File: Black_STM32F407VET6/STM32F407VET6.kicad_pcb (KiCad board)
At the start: 2 copper layers, 96 parts, among them J1 T0, J10 - HotBed +, J11 Heater0, J12 X-, J13 Y-, J14 Z-, J15 Z+, J16 USB_B, J17 LeftSpi, J18 EXTRAPINS, J2 T1, J23 EXP2, J24 LCD2004, J25 Bottom, J26 Right, J28 LIGHTS, J29 Z, J3 TB, J30 Z, J38 X, J39 Y, J4 TC, J41 E0, J43 Heater1, J44 COM, J47 I2C, J48 SPI, J49 SPI, J5 + VIN -, J50 SDIO, J51 Servo, J52 Servo, J53 PowerSelect, J54 Power, J55 PD11, J56 Power, J6 Fan3, J7 Fan2, J8 Fan1, J9 Fan0, Q1 BCX70, Q10 BCX70, Q11 BCX70, Q12 IRLR8726PBF, Q13 IRLR8726PBF, Q14 IRLR8726PBF, Q2 BCX70, Q3 BCX70, Q4 IRLML0030TRPBF, Q5 BCX70, Q6 IRLML0030TRPBF, Q7 IRLML0030TRPBF, Q8 IRLML0030TRPBF, Q9 BCX70, SW1 Boot0, U1 LeftAnalog, U2 Left5V, U5 AT24CS01-SSHM

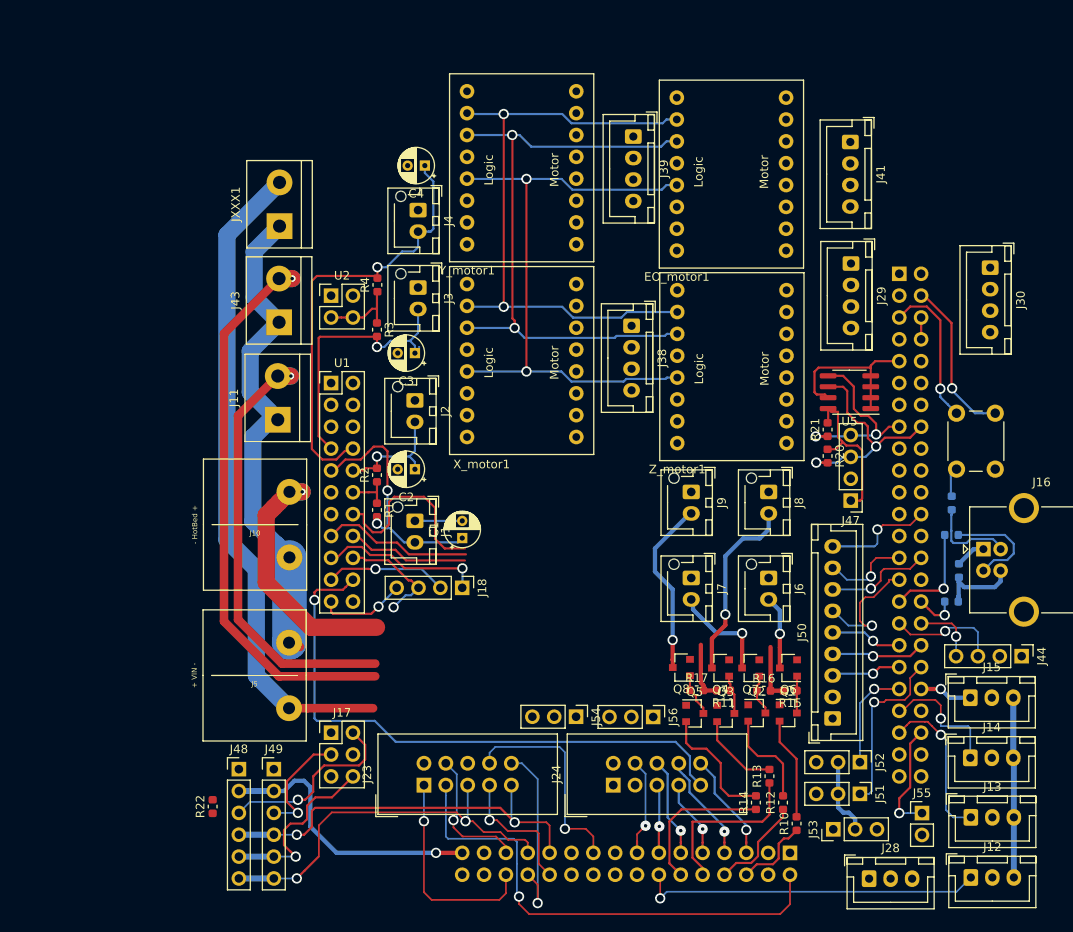
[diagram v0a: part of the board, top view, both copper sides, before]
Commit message: Wider tracks, more clearance, X & Y logic. 	SPI 1 is no longer used on shield because is used on the mcu board with different pins 	Added a design rule, distance between tracks is now at least 0.2925 	Wired X and Y driver logic with pin changes. 	Added a buck convertor spot with external connections in the meantime 	Stepper drivers are now consistently spaced from each other.
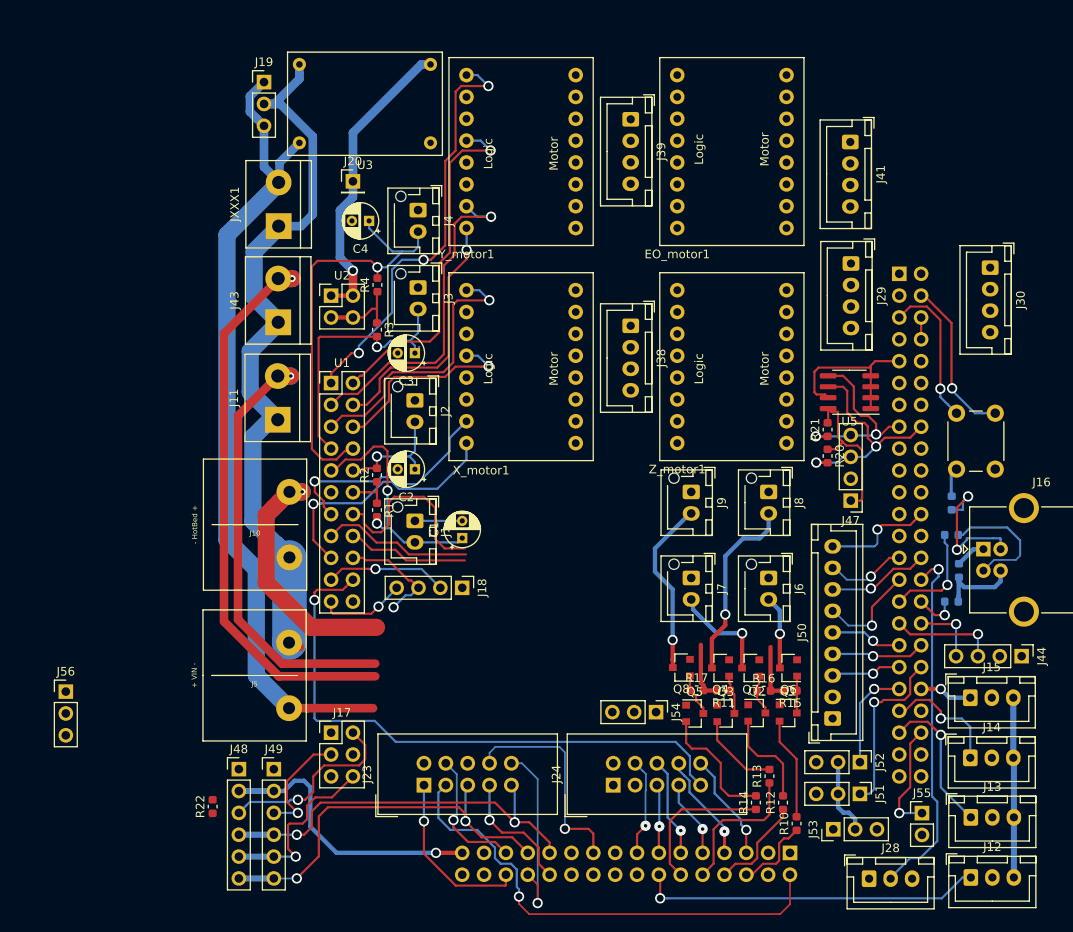
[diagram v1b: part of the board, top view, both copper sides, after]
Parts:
- added J19: 12Vinput, Connector_PinHeader_2.54mm:PinHeader_1x03_P2.54mm_Vertical, F.Cu at (114.1, 61.5)
- added J20: 5VOut, Connector_PinHeader_2.54mm:PinHeader_1x01_P2.54mm_Vertical, F.Cu at (124.5, 73.1)
- added U3: BuckConvertor, Motor_driver:MP2307Buck, F.Cu at (125.9, 64.1)
- moved J56 68.3 mm to (91.1, 132.4), turned to 0 degrees
- moved J54 9.31 mm to (159.7, 134.8)
- moved C4 9.12 mm to (126.3, 77.7)
- moved EO_motor1 2.62 mm to (160.1, 80.5)
- moved J39 2.03 mm to (156.7, 65.9)
- moved Y_motor1 1.89 mm to (135.6, 80.5)
- moved X_motor1 0.71 mm to (135.6, 105.5)
- moved JXXX1 0.10 mm to (115.8, 78.3)
- moved J43 0.10 mm to (115.8, 89.5)
- moved J38 0.10 mm to (156.7, 89.9)
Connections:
- J10 pad 1: Net-(J10-Pad1) -> 12V
- J18 pad 1: PA4 -> PD6
- J26 pad 20: Y_En -> PD6
- Q12 pad 2: Net-(Q12-Pad2) -> Net-(J10-Pad2)
- U1 pad 1: X_Step -> Y_En
- U1 pad 13: X_Dir -> X_Step
- U1 pad 17: PA4 -> X_Dir
- U1 pad 3: X_CS -> Y_Step
- U1 pad 4: Y_Step -> Y_Dir
- U1 pad 6: Y_Dir -> X_CS
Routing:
- net CLK: track 119.9 -> 46.3 mm, vias 4 -> 2
- net MISO: track 116.4 -> 43.4 mm, vias 4 -> 2
- net MOSI: track 118.6 -> 46.7 mm, vias 4 -> 2
- net Y_En: track 0.00 -> 49.5 mm, vias 0 -> 3
- net LIGHT_DIN: track 0.00 -> 42.0 mm, vias 0 -> 1
- net Y_CS: track 0.00 -> 41.3 mm, vias 0 -> 1
- net Y_Step: track 0.00 -> 39.2 mm, vias 0 -> 1
- net 5V: track 24.5 -> 59.5 mm, vias 0 -> 1
- net X_En: track 0.00 -> 32.6 mm, vias 0 -> 1
- net X_Dir: track 0.04 -> 30.3 mm, vias 0 -> 1
- net Y_Dir: track 0.00 -> 30.1 mm, vias 0 -> 1
- net 12V: track 132.6 -> 160.4 mm
- net X_Step: track 0.00 -> 26.7 mm, vias 0 -> 1
- net GND: track 114.3 -> 140.3 mm, vias 0 -> 2
- net X_CS: track 0.00 -> 23.0 mm, vias 0 -> 1
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
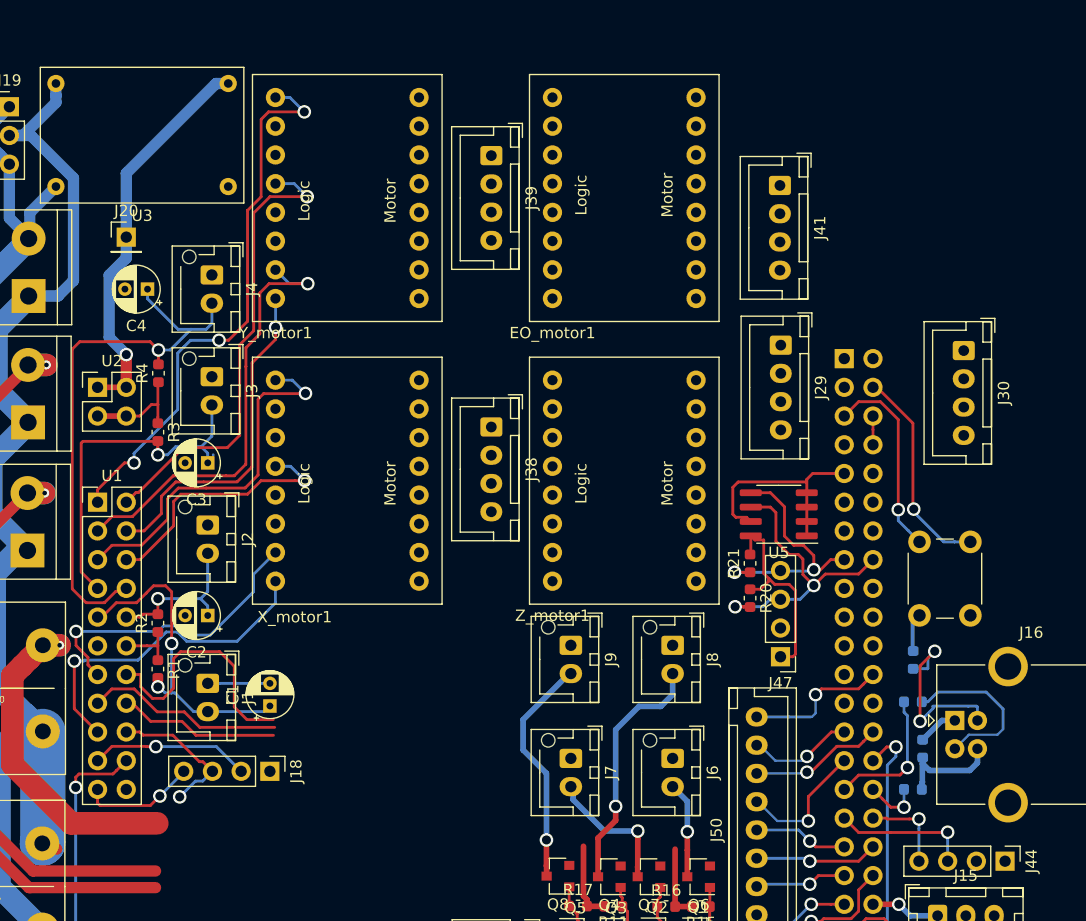
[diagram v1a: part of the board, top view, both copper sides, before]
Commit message: Z and E0 wiring 	- 12V rails 	- TODO: spi lines
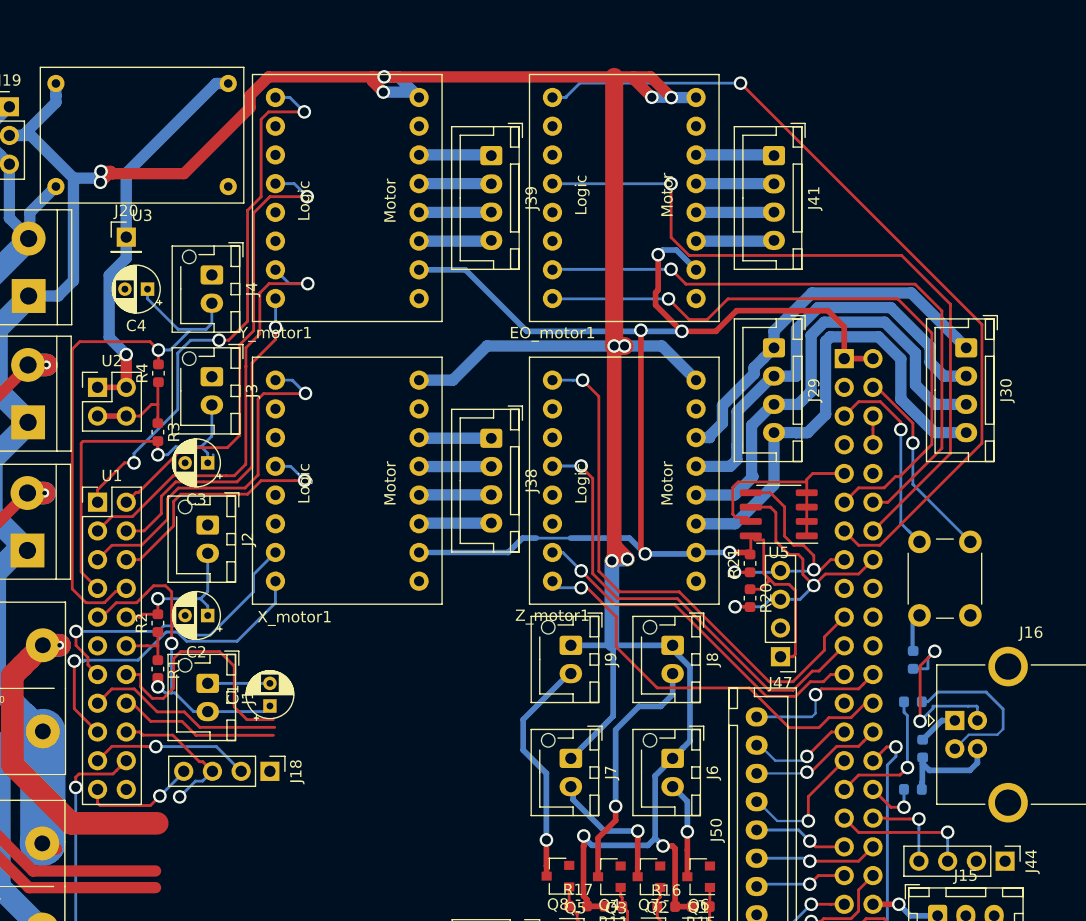
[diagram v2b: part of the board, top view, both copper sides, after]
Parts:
- moved J41 2.69 mm to (181.7, 65.9)
- moved J38 1.00 mm to (156.7, 90.9)
- moved J29 0.65 mm to (181.7, 82.9)
- moved J30 0.33 mm to (198.7, 82.9)
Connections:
- J26 pad 11: Z_En -> E0_Dir
- J26 pad 12: E0_En -> E0_Step
- J26 pad 13: Z_CS -> E0_En
- J26 pad 19: E0_Step -> Z_En
- J26 pad 21: Z_Step -> Z_CS
- J26 pad 23: E0_Dir -> Z_Step
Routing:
- net 12V: track 160.4 -> 367.1 mm, vias 1 -> 13
- net 3V3: track 84.7 -> 192.5 mm, vias 2 -> 7
- net E0_En: track 0.00 -> 74.3 mm, vias 0 -> 1
- net E0_CS: track 0.00 -> 65.3 mm, vias 0 -> 1
- net E0_Step: track 0.00 -> 56.2 mm, vias 0 -> 1
- net E0_Dir: track 0.00 -> 56.1 mm, vias 0 -> 1
- net Z_En: track 0.00 -> 49.0 mm, vias 0 -> 1
- net Net-(J29-Pad4): track 0.00 -> 42.8 mm
- net Net-(J29-Pad3): track 0.00 -> 40.6 mm
- net Z_CS: track 0.00 -> 40.6 mm, vias 0 -> 1
- net Net-(J29-Pad2): track 0.00 -> 37.9 mm
- net Z_Dir: track 0.00 -> 36.2 mm, vias 0 -> 1
- net Net-(J29-Pad1): track 0.00 -> 33.4 mm
- net Z_Step: track 0.00 -> 31.9 mm, vias 0 -> 1
- net Net-(EO_motor1-Pad14): track 0.00 -> 6.92 mm
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
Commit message: Power lines
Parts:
- moved C9 95.7 mm to (77.8, 134.8), turned to 270 degrees
- moved Q12 94.8 mm to (152.6, 113.9), turned to 0 degrees
- moved Q14 90.5 mm to (152.6, 120.9), turned to 0 degrees
- moved Q9 88.9 mm to (148.8, 115.7), turned to 270 degrees
- moved R28 87.9 mm to (151.4, 122.8), turned to 90 degrees
- moved R26 87.4 mm to (149.3, 119.0), turned to 270 degrees
- moved Q13 87.2 mm to (152.6, 127.9), turned to 0 degrees
- moved R25 85.4 mm to (147.8, 119.0), turned to 270 degrees
- moved Q11 84.8 mm to (148.8, 122.3), turned to 270 degrees
- moved R27 81.6 mm to (147.8, 125.9), turned to 90 degrees
- moved Q10 81.4 mm to (148.8, 129.4), turned to 270 degrees
- moved R23 71.3 mm to (142.7, 117.2)
- moved R24 71.3 mm to (142.7, 115.4)
- moved J56 54.2 mm to (145.2, 135.1), turned to 90 degrees
- moved C10 22.8 mm to (68.8, 134.9)
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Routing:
- net 5V: track 59.5 -> 319.8 mm, vias 1 -> 3
- net MOSI: track 46.7 -> 205.5 mm, vias 2 -> 6
- net CLK: track 46.3 -> 198.0 mm, vias 2 -> 6
- net MISO: track 43.4 -> 193.6 mm, vias 2 -> 6
- net 3V3: track 192.5 -> 322.2 mm, vias 7 -> 9
- net PD6: track 0.04 -> 89.9 mm, vias 0 -> 1
- net 12V: track 367.1 -> 326.4 mm
- net EN2: track 0.00 -> 22.0 mm, vias 0 -> 1
- net GND: track 140.3 -> 152.2 mm
- net Net-(J43-Pad2): track 72.8 -> 65.8 mm
- net Net-(J10-Pad2): track 36.7 -> 29.6 mm
- net Net-(J11-Pad2): track 58.3 -> 51.3 mm
- net X_Step: track 26.7 -> 27.7 mm

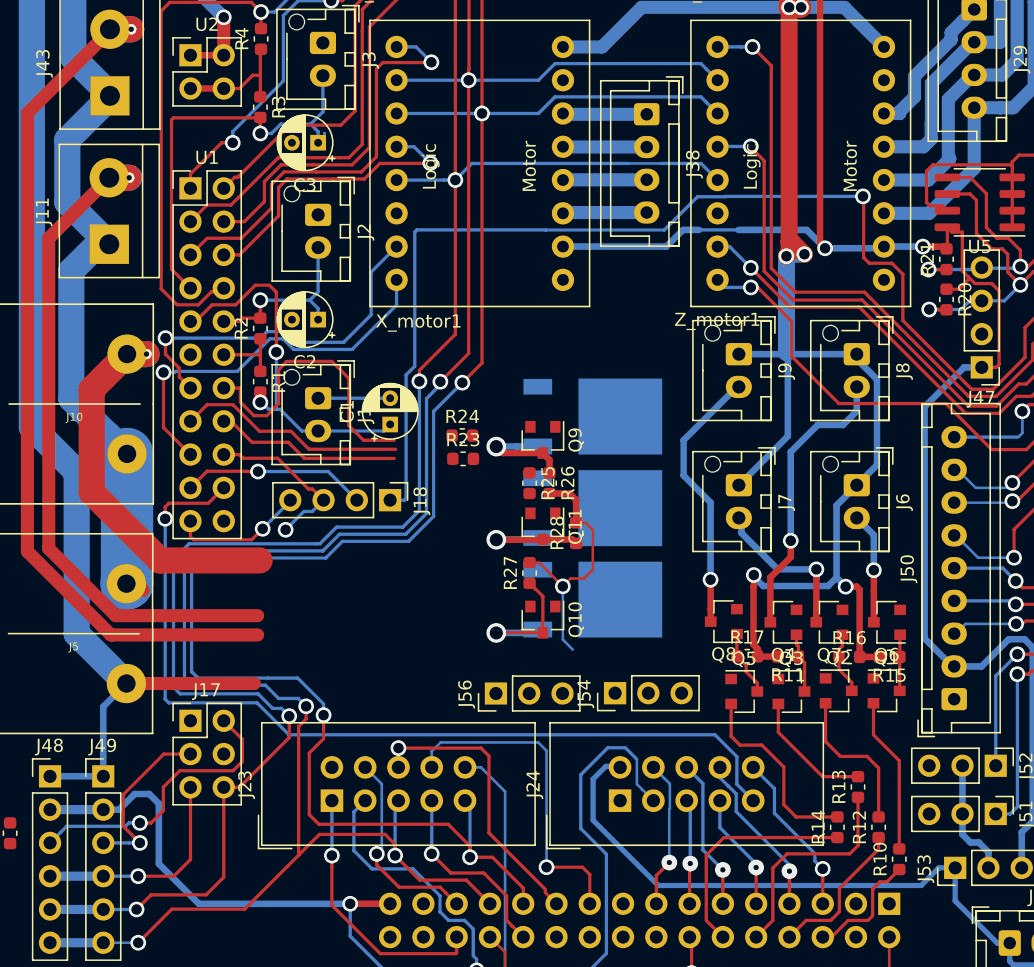
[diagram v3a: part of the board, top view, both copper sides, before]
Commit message: Power mosfets  - everything done apart from connecting GND  - Are the 12V rail caps necessary ?
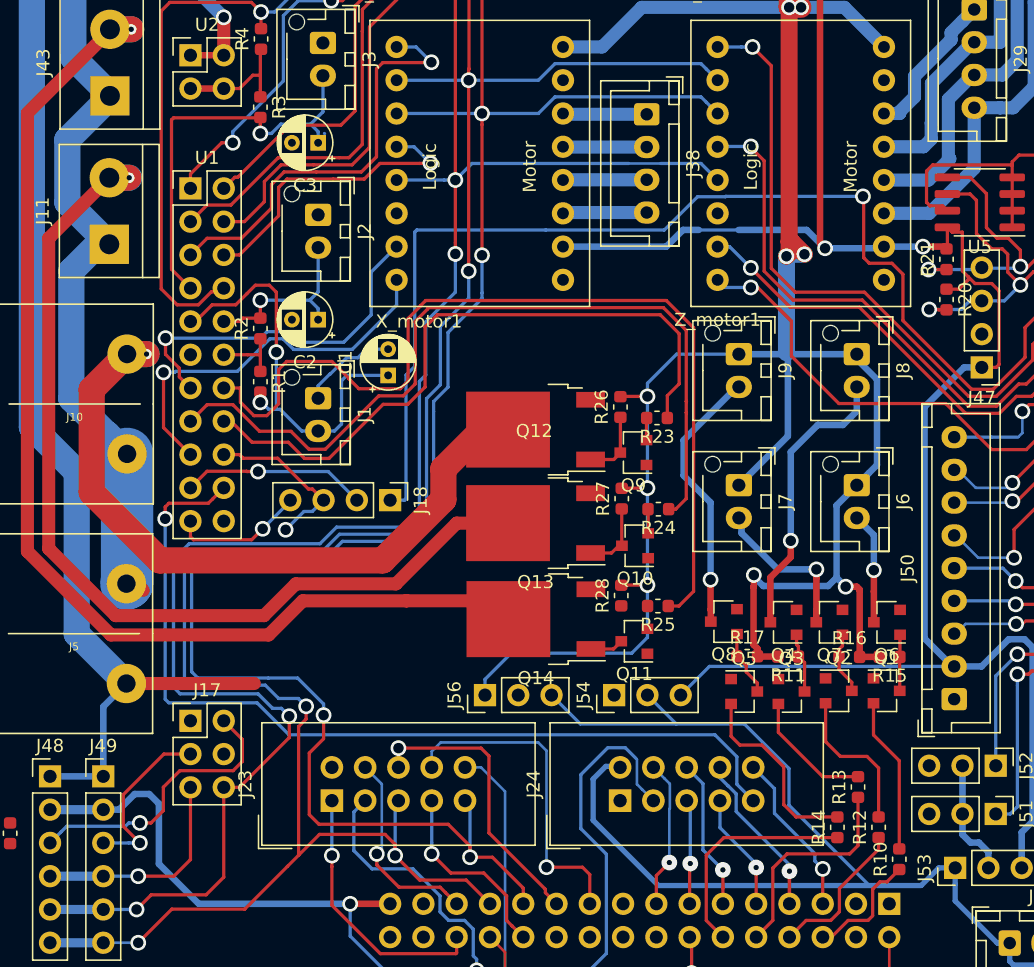
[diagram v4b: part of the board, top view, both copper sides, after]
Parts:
- Q12, Q13, Q14: moved to F.Cu
- moved R24 16.0 mm to (157.6, 121.0), turned to 180 degrees
- moved R23 15.1 mm to (157.5, 114.0), turned to 180 degrees
- moved R25 13.6 mm to (157.6, 128.4), turned to 180 degrees
- moved Q11 11.2 mm to (155.8, 131.1), turned to 180 degrees
- moved Q14 9.52 mm to (148.3, 129.4), turned to 180 degrees
- moved R27 9.04 mm to (154.8, 120.2)
- moved Q10 9.02 mm to (155.9, 123.8), turned to 180 degrees
- moved R26 7.94 mm to (154.7, 113.2), turned to 90 degrees
- moved Q13 7.29 mm to (148.3, 122.1), turned to 180 degrees
- moved Q9 6.98 mm to (155.7, 116.7), turned to 180 degrees
- moved R28 5.88 mm to (154.8, 127.6)
- moved Q12 4.48 mm to (148.3, 114.9), turned to 180 degrees
- moved C1 3.75 mm to (137.0, 110.8)
- moved J56 0.85 mm to (144.4, 135.2)
- moved J54 0.16 mm to (154.3, 135.2)
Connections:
- U1 pad 14: HotBed -> Heater1
- U1 pad 16: Heater1 -> HotBed
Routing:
- net Heater1: track 14.2 -> 70.5 mm
- net Heater0: track 17.6 -> 62.3 mm
- net 5V: track 319.8 -> 355.2 mm
- net 12V: track 326.4 -> 354.9 mm, vias 13 -> 15
- net HotBed: track 22.4 -> 50.6 mm
- net Net-(J10-Pad2): track 29.6 -> 54.1 mm
- net Net-(J11-Pad2): track 51.3 -> 73.3 mm
- net 3V3: track 322.2 -> 344.0 mm
- net Net-(J43-Pad2): track 65.8 -> 86.6 mm
- net Net-(Q11-Pad3): track 9.45 -> 2.56 mm, vias 1 -> 0
- net Net-(Q10-Pad3): track 11.0 -> 5.35 mm, vias 1 -> 0
- net T0: track 28.7 -> 32.0 mm
- net Net-(Q12-Pad1): track 8.47 -> 5.20 mm, vias 1 -> 0
- net GND: track 152.2 -> 154.2 mm
- net Net-(Q10-Pad2): track 0.00 -> 1.85 mm
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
